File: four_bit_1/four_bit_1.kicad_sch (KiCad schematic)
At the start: 69 parts

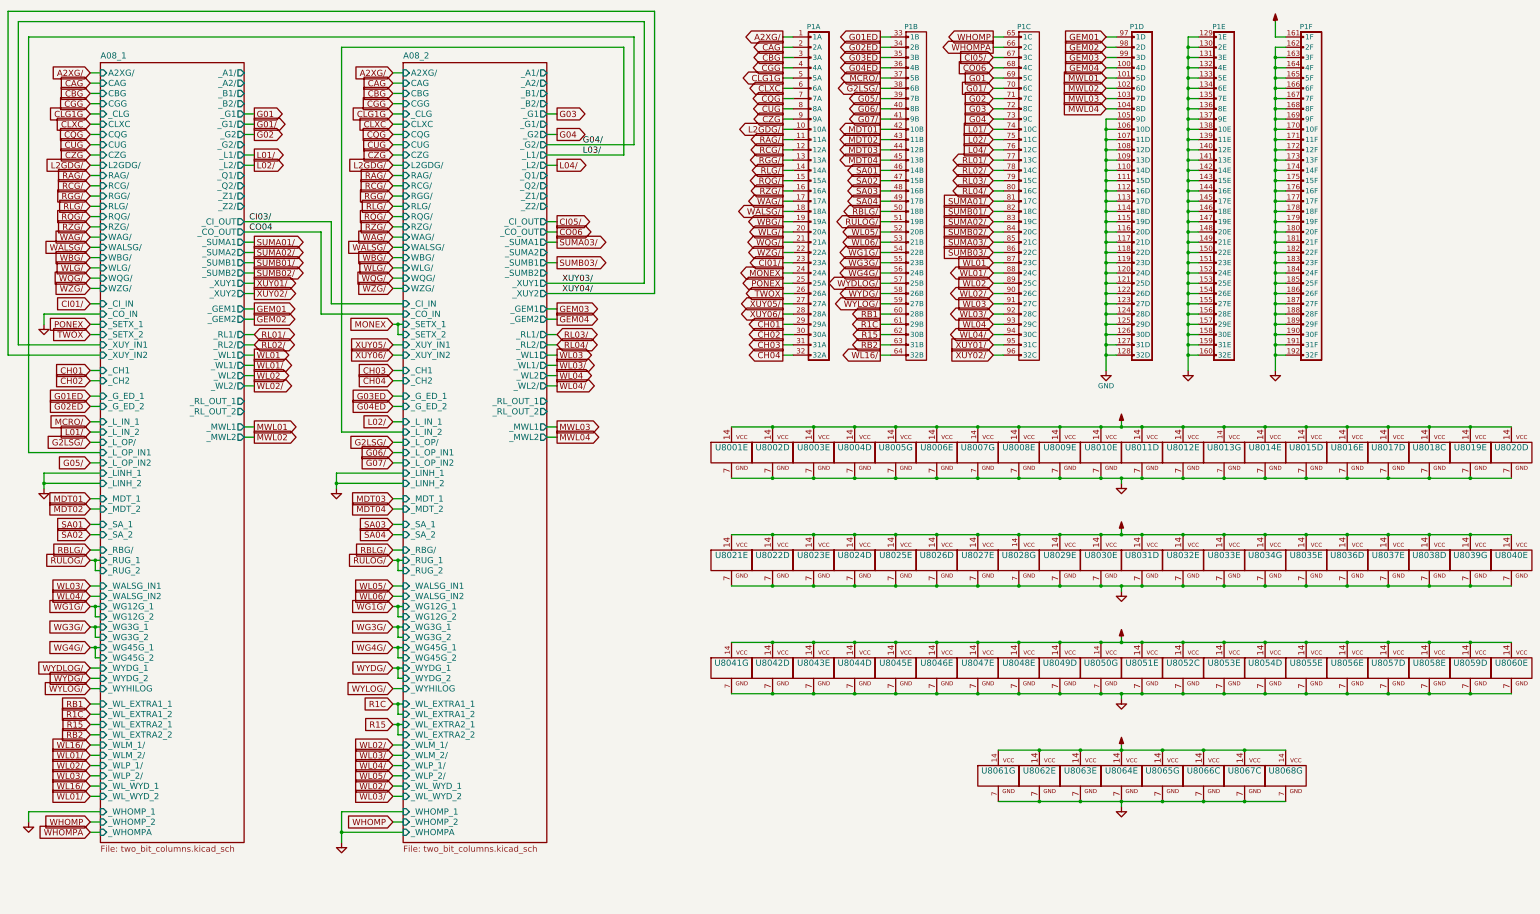
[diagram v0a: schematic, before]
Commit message: Generic 4 Bit Adder schematic + pcb
Generic 4 Bit Adder schematic + pcb 
rev a
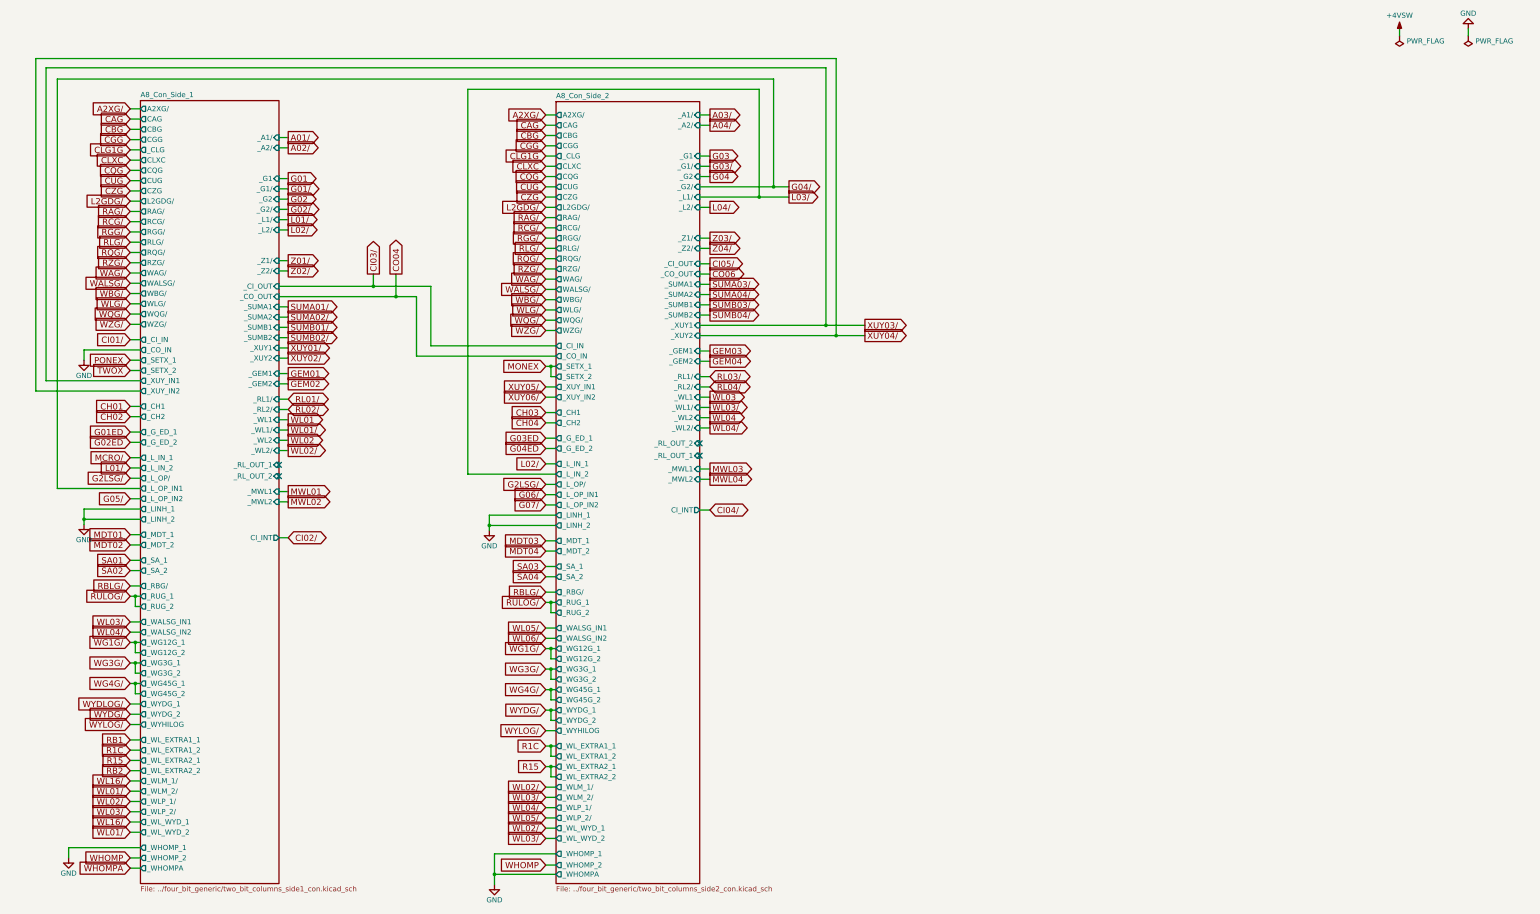
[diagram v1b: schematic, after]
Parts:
- removed P1: (no value), symbol agc_kicad_components:DIN_41612_128P
- removed U8001, U8003, U8006, U8008, U8009, U8010, U8012, U8014, U8016, U8019, U8021, U8023, U8025, U8027, U8029, U8030, U8032, U8033, U8035, U8037, U8040, U8043, U8045, U8046, U8047, U8048, U8051, U8053, U8055, U8056, U8058, U8060, U8062, U8063, U8064: (no value), symbol agc_kicad_components:74HC02
- removed U8002, U8004, U8011, U8015, U8017, U8020, U8022, U8024, U8026, U8031, U8036, U8038, U8042, U8044, U8049, U8054, U8057, U8059: (no value), symbol agc_kicad_components:74HC27
- removed U8005, U8034, U8039, U8065: (no value), symbol agc_kicad_components:74HC04
- removed U8007, U8013, U8028, U8041, U8050, U8061: (no value), symbol agc_kicad_components:74LVC07
- removed U8018, U8052, U8066, U8067: (no value), symbol agc_kicad_components:74HC4002
- removed U8068: (no value), symbol agc_kicad_components:74LVC06
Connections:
- no-connect marks 0 -> 4
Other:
- removed sheet A08_1
- removed sheet A08_2
- added sheet A8_Con_Side_1 (../four_bit_generic/two_bit_columns_side1_con.kicad_sch)
- added sheet A8_Con_Side_2 (../four_bit_generic/two_bit_columns_side2_con.kicad_sch)
